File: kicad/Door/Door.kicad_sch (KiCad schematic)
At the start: 14 parts, among them Q1 Q_NMOS_GDS, Q2 Q_PMOS_GSD, SW1 SW_Push, SW2 USB/BAT, SW3 RST_BTN, U1 NODEMCU v3

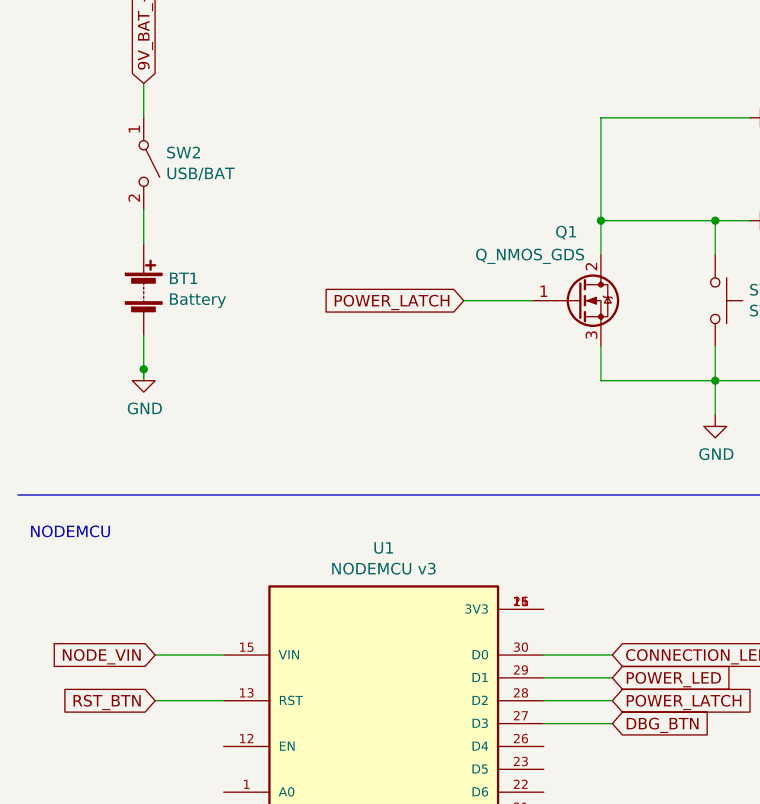
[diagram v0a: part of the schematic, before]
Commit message: Kicad: Door: Fixed bottom plane not connected to GND net + Changed USB/BAT to BAT CON/DISCON on SW2 + Added labels for SW2 + Moved github link and board name to backside
Signed-off-by: CTXz <ctx.xda@gmail.com>
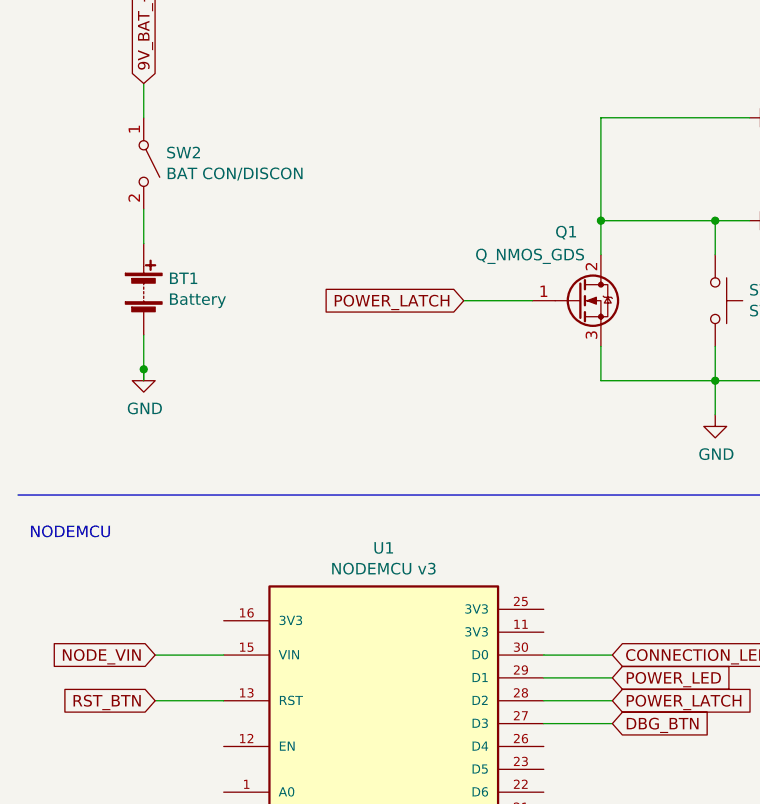
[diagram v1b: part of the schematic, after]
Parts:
- SW2: value USB/BAT -> BAT CON/DISCON
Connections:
- now unconnected: U1.11 (3V3), U1.16 (3V3), U1.25 (3V3)
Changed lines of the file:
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@@
       (effects (font (size 1.27 1.27)) (justify left))
     )
-    (property "Value" "USB/BAT" (id 1) (at 29.1592 39.243 90)
+    (property "Value" "BAT CON/DISCON" (id 1) (at 29.1592 39.243 90)
       (effects (font (size 1.27 1.27)) (justify left))
     )
@@
     )
     (path "/00000000-0000-0000-0000-000061df5f15"
-      (reference "SW2") (unit 1) (value "USB/BAT") (footprint "digikey-footprints:Toggle_Switch_100SP1T1B4M2QE")
+      (reference "SW2") (unit 1) (value "BAT CON/DISCON") (footprint "digikey-footprints:Toggle_Switch_100SP1T1B4M2QE")
     )
     (path "/00000000-0000-0000-0000-000061e06f44"
